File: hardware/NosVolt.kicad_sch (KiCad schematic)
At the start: 18 parts, among them J101 INPUTS, J102 OUTPUTS, SW101 SW_Reset, SW102 SSSS811101, U101 GMT028-05, U102 ESP32-S3-WROOM-1

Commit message: Test points
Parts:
- added C104: 100nF, Capacitor_SMD:C_0603_1608Metric, symbol Device:C
- added J103: BAT_NTC, Connector_JST:JST_GH_SM03B-GHS-TB_1x03-1MP_P1.25mm_Horizontal, symbol Connector_Generic_MountingPin:Conn_01x03_MountingPin
- added R105: 4.7K, Resistor_SMD:R_0603_1608Metric_Pad0.98x0.95mm_HandSolder, symbol Device:R
- added TP_101: BOOT, NosLib:TestPoint_Pad_1.0x1.0mm, symbol Connector:TestPoint
- added TP_102: +5V_USB, NosLib:TestPoint_Pad_1.0x1.0mm, symbol Connector:TestPoint
- added TP_103: SDA, NosLib:TestPoint_Pad_1.0x1.0mm, symbol Connector:TestPoint
- added TP_104: SCL, NosLib:TestPoint_Pad_1.0x1.0mm, symbol Connector:TestPoint
- added TP_105, TP_116: GND, NosLib:TestPoint_Pad_1.0x1.0mm, symbol Connector:TestPoint
- added TP_106: MTCK, NosLib:TestPoint_Pad_1.0x1.0mm, symbol Connector:TestPoint
- added TP_107: MTDO, NosLib:TestPoint_Pad_1.0x1.0mm, symbol Connector:TestPoint
- added TP_108: MTDI, NosLib:TestPoint_Pad_1.0x1.0mm, symbol Connector:TestPoint
- added TP_109: MTMS, NosLib:TestPoint_Pad_1.0x1.0mm, symbol Connector:TestPoint
- added TP_110: DALLAS, NosLib:TestPoint_Pad_1.0x1.0mm, symbol Connector:TestPoint
- added TP_112: TX, NosLib:TestPoint_Pad_1.0x1.0mm, symbol Connector:TestPoint
- added TP_113: RX, NosLib:TestPoint_Pad_1.0x1.0mm, symbol Connector:TestPoint
- added TP_115: +3V3_USB, NosLib:TestPoint_Pad_1.0x1.0mm, symbol Connector:TestPoint
- added TP_117: +3V3_UPS, NosLib:TestPoint_Pad_1.0x1.0mm, symbol Connector:TestPoint
- added TP_118: +12V_UPS, NosLib:TestPoint_Pad_1.0x1.0mm, symbol Connector:TestPoint
- added TP_123: +3V3, NosLib:TestPoint_Pad_1.0x1.0mm, symbol Connector:TestPoint
- added U102: DS18B20Z, Package_SO:SOIC-8_3.9x4.9mm_P1.27mm, symbol Sensor_Temperature:DS18B20Z
- renumbered U102 to U103
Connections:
- net SHUNT_OUT_LO is gone; now on net SHUNT_OUT_HI: J101.1 (Pin_1), NT101.2
- net +12V_UPS: now also TP_118.1
- net +3V3: now also C104.1, J103.3 (Pin_3), R105.2, TP_123.1, U102.3 (V_{DD})
- net +3V3_UPS: now also TP_117.1
- net +3V3_USB: now also TP_115.1
- net BOOT: now also TP_101.1
- net GND: now also C104.2, J103.1 (Pin_1), J103.MP (MountPin), TP_105.1, TP_116.1, U102.5 (GND)
- net SCL: now also TP_103.1
- net SDA: now also TP_104.1
- net SHUNT_OUT_HI: no longer J101.2 (Pin_2), J102.2 (Pin_2), J102.4 (Pin_4), J102.6 (Pin_6)
- net USB_LDO/USB_5V: now also TP_102.1
- net DALLAS: now reaches U103.31 (GPIO38/FSPIWP/SUBSPIWP)
- net DALLAS: now also J103.2 (Pin_2), R105.1, TP_110.1, U102.4 (DQ)
- net at U103.32 (MTCK/GPIO39/CLK_OUT3/SUBSPICS1): now also TP_106.1
- net at U103.33 (MTDO/GPIO40/CLK_OUT2): now also TP_107.1
- net at U103.34 (MTDI/GPIO41/CLK_OUT1): now also TP_108.1
- net at U103.35 (MTMS/GPIO42): now also TP_109.1
- net at U103.36 (U0RXD/GPIO44/CLK_OUT2): now also TP_113.1
- net at U103.37 (U0TXD/GPIO43/CLK_OUT1): now also TP_112.1
- net SHUNT_OUT_LO1 renamed SHUNT_USP_LO1
- net SHUNT_OUT_LO2 renamed SHUNT_LO_OUT2
- net SHUNT_OUT_LO3 renamed SHUNT_USP_LO3
- new net SHUNT_GND: J101.2 (Pin_2), J102.2 (Pin_2), J102.4 (Pin_4), J102.6 (Pin_6)
- no-connect marks 6 -> 11
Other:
- moved on the sheet: H101, H102, H103, H104, J101, J102, NT101, R101, R103, R104, U101, U103

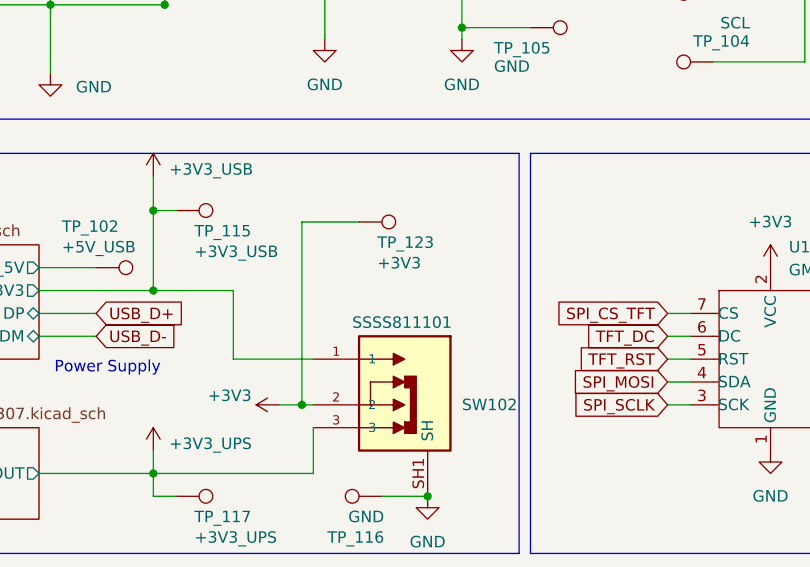
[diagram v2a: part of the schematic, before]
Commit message: hand soldering footprints and led
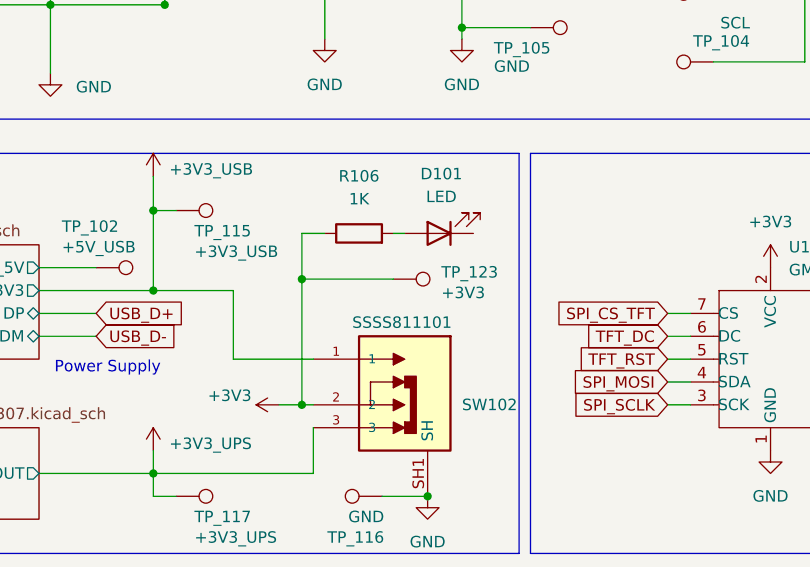
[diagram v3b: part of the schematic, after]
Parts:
- added D101: LED, LED_SMD:LED_0805_2012Metric_Pad1.15x1.40mm_HandSolder, symbol Device:LED
- added R106: 1K, Resistor_SMD:R_0603_1608Metric_Pad0.98x0.95mm_HandSolder, symbol Device:R
- C101, C103: footprint Capacitor_SMD:C_0805_2012Metric -> Capacitor_SMD:C_0805_2012Metric_Pad1.18x1.45mm_HandSolder
- C102, C104: footprint Capacitor_SMD:C_0603_1608Metric -> Capacitor_SMD:C_0603_1608Metric_Pad1.08x0.95mm_HandSolder
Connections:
- net +3V3: now also R106.1
- new net: D101.2 (A), R106.2
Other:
- moved on the sheet: TP_123
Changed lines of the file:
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@@
 	)
 	(junction
+		(at 85.09 76.2)
+		(diameter 0)
+		(color 0 0 0 0)
+	)
+	(junction
 		(at 119.38 30.48)
 		(diameter 0)
@@
 	(wire
 		(pts
+			(xy 95.25 71.12) (xy 96.52 71.12)
+		)
+		(stroke
+			(width 0)
+			(type default)
+		)
+	)
+	(wire
+		(pts
 			(xy 35.56 163.83) (xy 35.56 170.18)
 		)
@@
 	(wire
 		(pts
+			(xy 85.09 71.12) (xy 85.09 76.2)
+		)
+		(stroke
+			(width 0)
+			(type default)
+		)
+	)
+	(wire
+		(pts
 			(xy 140.97 52.07) (xy 140.97 30.48)
 		)
@@
 	(wire
 		(pts
-			(xy 91.44 69.85) (xy 85.09 69.85)
+			(xy 95.25 76.2) (xy 85.09 76.2)
 		)
 		(stroke
@@
 	(wire
 		(pts
-			(xy 85.09 69.85) (xy 85.09 90.17)
+			(xy 85.09 76.2) (xy 85.09 90.17)
 		)
 		(stroke
@@
 	(wire
 		(pts
+			(xy 87.63 71.12) (xy 85.09 71.12)
+		)
+		(stroke
+			(width 0)
+			(type default)
+		)
+	)
+	(wire
+		(pts
 			(xy 55.88 77.47) (xy 68.58 77.47)
 		)
@@
 			)
 		)
-		(property "Footprint" "Capacitor_SMD:C_0805_2012Metric"
+		(property "Footprint" "Capacitor_SMD:C_0805_2012Metric_Pad1.18x1.45mm_HandSolder"
 			(at 103.8352 44.45 0)
 			(effects
@@
 			)
 		)
-		(property "Footprint" "Capacitor_SMD:C_0805_2012Metric"
+		(property "Footprint" "Capacitor_SMD:C_0805_2012Metric_Pad1.18x1.45mm_HandSolder"
 			(at 58.1152 44.45 0)
 			(effects
@@
 	)
 	(symbol
+		(lib_id "Device:R")
+		(at 91.44 71.12 90)
+		(unit 1)
+		(exclude_from_sim no)
+		(in_bom yes)
+		(on_board yes)
+		(dnp no)
+		(fields_autoplaced yes)
+		(property "Reference" "R106"
+			(at 91.44 64.77 90)
+			(effects
+				(font
+					(size 1.27 1.27)
+				)
+			)
+		)
+		(property "Value" "1K"
+			(at 91.44 67.31 90)
+			(effects
+				(font
+					(size 1.27 1.27)
+				)
+			)
+		)
+		(property "Footprint" "Resistor_SMD:R_0603_1608Metric_Pad0.98x0.95mm_HandSolder"
+			(at 91.44 72.898 90)
+			(effects
+				(font
+					(size 1.27 1.27)
+				)
+				(hide yes)
+			)
+		)
+		(property "Datasheet" "~"
+			(at 91.44 71.12 0)
+			(effects
+				(font
+					(size 1.27 1.27)
+				)
+				(hide yes)
+			)
+		)
+		(property "Description" "Resistor"
+			(at 91.44 71.12 0)
+			(effects
+				(font
+					(size 1.27 1.27)
+				)
+				(hide yes)
+			)
+		)
+		(pin "2"
+		)
+		(pin "1"
+		)
+		(instances
+			(project "NosVolt"
+				(path "/2a3ef4c2-927a-45cd-a4f2-5ee83a7e9444"
+					(reference "R106")
+					(unit 1)
+				)
+			)
+		)
+	)
+	(symbol
 		(lib_id "NosLib:SSSS811101")
 		(at 96.52 87.63 0)
@@
 	(symbol
 		(lib_id "Connector:TestPoint")
-		(at 91.44 69.85 270)
+		(at 95.25 76.2 270)
 		(unit 1)
 		(exclude_from_sim no)
@@
 		(dnp no)
 		(property "Reference" "TP_123"
-			(at 93.472 72.136 90)
+			(at 100.584 75.438 90)
 			(effects
 				(font
@@
 		)
 		(property "Value" "+3V3"
-			(at 93.472 74.422 90)
+			(at 100.584 77.724 90)
 			(effects
 				(font
@@
 		)
 		(property "Footprint" "NosLib:TestPoint_Pad_1.0x1.0mm"
-			(at 91.44 74.93 0)
+			(at 95.25 81.28 0)
 			(effects
 				(font
@@
 		)
 		(property "Datasheet" "~"
-			(at 91.44 74.93 0)
+			(at 95.25 81.28 0)
 			(effects
 				(font
@@
 		)
 		(property "Description" "test point"
-			(at 91.44 69.85 0)
+			(at 95.25 76.2 0)
 			(effects
 				(font
@@
 	)
 	(symbol
+		(lib_id "Device:LED")
+		(at 100.33 71.12 180)
+		(unit 1)
+		(exclude_from_sim no)
+		(in_bom yes)
+		(on_board yes)
+		(dnp no)
+		(property "Reference" "D101"
+			(at 100.584 64.516 0)
+			(effects
+				(font
+					(size 1.27 1.27)
+				)
+			)
+		)
+		(property "Value" "LED"
+			(at 100.584 67.056 0)
+			(effects
+				(font
+					(size 1.27 1.27)
+				)
+			)
+		)
+		(property "Footprint" "LED_SMD:LED_0805_2012Metric_Pad1.15x1.40mm_HandSolder"
+			(at 100.33 71.12 0)
+			(effects
+				(font
+					(size 1.27 1.27)
+				)
+				(hide yes)
+			)
+		)
+		(property "Datasheet" "~"
+			(at 100.33 71.12 0)
+			(effects
+				(font
+					(size 1.27 1.27)
+				)
+				(hide yes)
+			)
+		)
+		(property "Description" "Light emitting diode"
+			(at 100.33 71.12 0)
+			(effects
+				(font
+					(size 1.27 1.27)
+				)
+				(hide yes)
+			)
+		)
+		(property "Sim.Pins" "1=K 2=A"
+			(at 100.33 71.12 0)
+			(effects
+				(font
+					(size 1.27 1.27)
+				)
+				(hide yes)
+			)
+		)
+		(pin "2"
+		)
+		(pin "1"
+		)
+		(instances
+			(project ""
+				(path "/2a3ef4c2-927a-45cd-a4f2-5ee83a7e9444"
+					(reference "D101")
+					(unit 1)
+				)
+			)
+		)
+	)
+	(symbol
 		(lib_id "power:+3.3V")
 		(at 68.58 64.77 0)
@@
 			)
 		)
-		(property "Footprint" "Capacitor_SMD:C_0603_1608Metric"
+		(property "Footprint" "Capacitor_SMD:C_0603_1608Metric_Pad1.08x0.95mm_HandSolder"
 			(at 199.39 152.7048 0)
 			(effects
@@
 			)
 		)
-		(property "Footprint" "Capacitor_SMD:C_0603_1608Metric"
+		(property "Footprint" "Capacitor_SMD:C_0603_1608Metric_Pad1.08x0.95mm_HandSolder"
 			(at 88.5952 44.45 0)
 			(effects

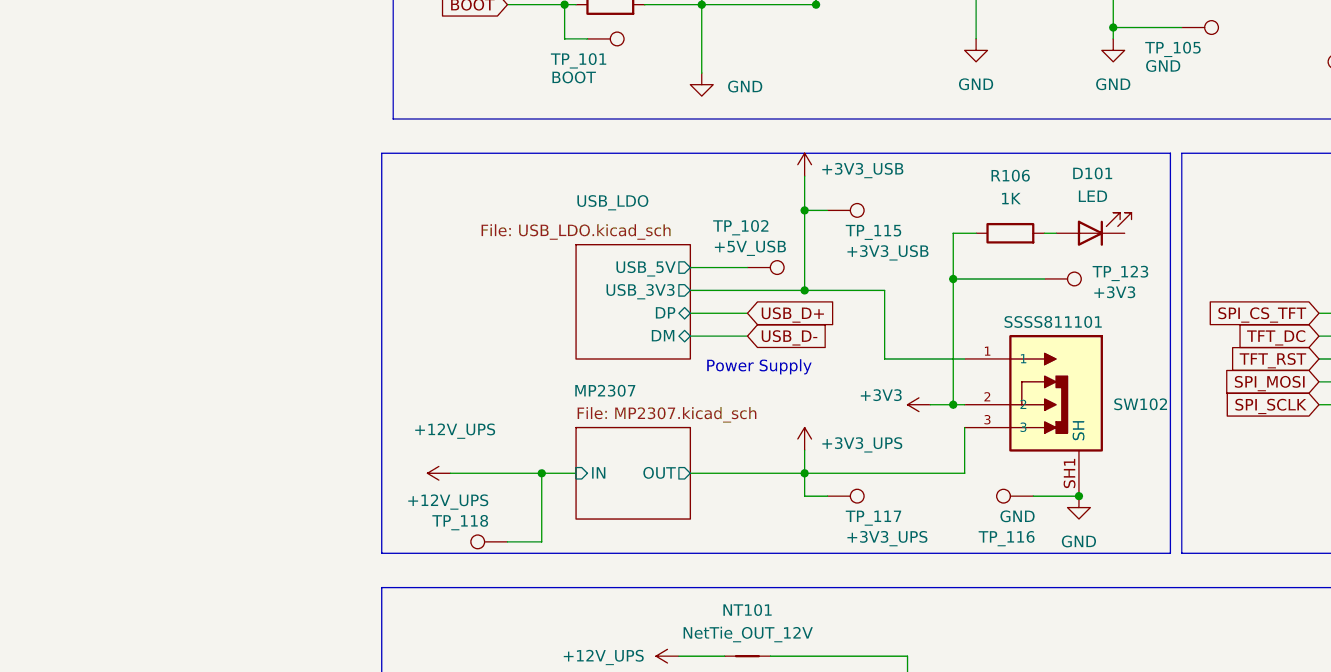
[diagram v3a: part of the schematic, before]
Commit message: hand soldering footprints and led
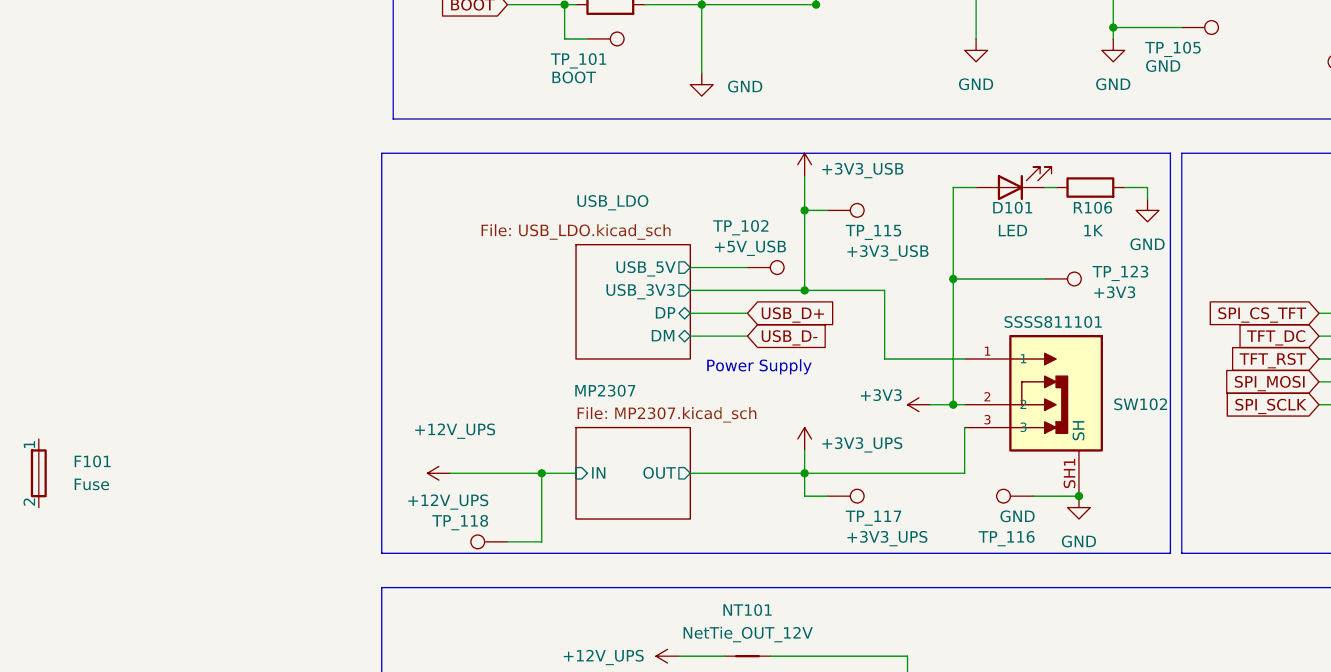
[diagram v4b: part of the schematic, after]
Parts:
- added F101: Fuse, NosLib:FUSE_3544-2, symbol Device:Fuse
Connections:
- net +3V3: now also D101.2 (A); no longer R106.1
- net GND: now also R106.2
- net at D101.1 (K): now also R106.1
- new net: F101.1_1 (1), F101.1_2 (1)
- new net: F101.2_1 (2), F101.2_2 (2)
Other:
- moved on the sheet: D101, R106
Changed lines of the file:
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@@
 	(wire
 		(pts
-			(xy 95.25 71.12) (xy 96.52 71.12)
+			(xy 95.25 66.04) (xy 96.52 66.04)
+		)
+		(stroke
+			(width 0)
+			(type default)
+		)
+	)
+	(wire
+		(pts
+			(xy 106.68 66.04) (xy 104.14 66.04)
 		)
 		(stroke
@@
 	(wire
 		(pts
-			(xy 85.09 71.12) (xy 85.09 76.2)
+			(xy 85.09 66.04) (xy 85.09 76.2)
 		)
 		(stroke
@@
 	(wire
 		(pts
+			(xy 106.68 66.04) (xy 106.68 67.31)
+		)
+		(stroke
+			(width 0)
+			(type default)
+		)
+	)
+	(wire
+		(pts
 			(xy 80.01 176.53) (xy 80.01 152.4)
 		)
@@
 	(wire
 		(pts
-			(xy 87.63 71.12) (xy 85.09 71.12)
+			(xy 87.63 66.04) (xy 85.09 66.04)
 		)
 		(stroke
@@
 	(symbol
 		(lib_id "Device:R")
-		(at 91.44 71.12 90)
+		(at 100.33 66.04 90)
 		(unit 1)
 		(exclude_from_sim no)
@@
 		(on_board yes)
 		(dnp no)
-		(fields_autoplaced yes)
 		(property "Reference" "R106"
-			(at 91.44 64.77 90)
+			(at 100.584 68.326 90)
 			(effects
 				(font
@@
 		)
 		(property "Value" "1K"
-			(at 91.44 67.31 90)
+			(at 100.584 70.866 90)
 			(effects
 				(font
@@
 		)
 		(property "Footprint" "Resistor_SMD:R_0603_1608Metric_Pad0.98x0.95mm_HandSolder"
-			(at 91.44 72.898 90)
+			(at 100.33 67.818 90)
 			(effects
 				(font
@@
 		)
 		(property "Datasheet" "~"
-			(at 91.44 71.12 0)
+			(at 100.33 66.04 0)
 			(effects
 				(font
@@
 		)
 		(property "Description" "Resistor"
-			(at 91.44 71.12 0)
+			(at 100.33 66.04 0)
 			(effects
 				(font
@@
 	(symbol
 		(lib_id "Device:LED")
-		(at 100.33 71.12 180)
+		(at 91.44 66.04 180)
 		(unit 1)
 		(exclude_from_sim no)
@@
 		(dnp no)
 		(property "Reference" "D101"
-			(at 100.584 64.516 0)
+			(at 91.694 68.326 0)
 			(effects
 				(font
@@
 		)
 		(property "Value" "LED"
-			(at 100.584 67.056 0)
+			(at 91.694 70.866 0)
 			(effects
 				(font
@@
 		)
 		(property "Footprint" "LED_SMD:LED_0805_2012Metric_Pad1.15x1.40mm_HandSolder"
-			(at 100.33 71.12 0)
+			(at 91.44 66.04 0)
 			(effects
 				(font
@@
 		)
 		(property "Datasheet" "~"
-			(at 100.33 71.12 0)
+			(at 91.44 66.04 0)
 			(effects
 				(font
@@
 		)
 		(property "Description" "Light emitting diode"
-			(at 100.33 71.12 0)
+			(at 91.44 66.04 0)
 			(effects
 				(font
@@
 		)
 		(property "Sim.Pins" "1=K 2=A"
-			(at 100.33 71.12 0)
+			(at 91.44 66.04 0)
 			(effects
 				(font
@@
 		)
 		(instances
-			(project ""
+			(project "NosVolt"
 				(path "/2a3ef4c2-927a-45cd-a4f2-5ee83a7e9444"
 					(reference "D101")
@@
 	)
 	(symbol
+		(lib_id "Device:Fuse")
+		(at -16.51 97.79 0)
+		(unit 1)
+		(exclude_from_sim no)
+		(in_bom yes)
+		(on_board yes)
+		(dnp no)
+		(fields_autoplaced yes)
+		(property "Reference" "F101"
+			(at -12.7 96.5199 0)
+			(effects
+				(font
+					(size 1.27 1.27)
+				)
+				(justify left)
+			)
+		)
+		(property "Value" "Fuse"
+			(at -12.7 99.0599 0)
+			(effects
+				(font
+					(size 1.27 1.27)
+				)
+				(justify left)
+			)
+		)
+		(property "Footprint" "NosLib:FUSE_3544-2"
+			(at -18.288 97.79 90)
+			(effects
+				(font
+					(size 1.27 1.27)
+				)
+				(hide yes)
+			)
+		)
+		(property "Datasheet" "~"
+			(at -16.51 97.79 0)
+			(effects
+				(font
+					(size 1.27 1.27)
+				)
+				(hide yes)
+			)
+		)
+		(property "Description" "Fuse"
+			(at -16.51 97.79 0)
+			(effects
+				(font
+					(size 1.27 1.27)
+				)
+				(hide yes)
+			)
+		)
+		(pin "2_1"
+		)
+		(pin "1_2"
+		)
+		(pin "2_2"
+		)
+		(pin "1_1"
+		)
+		(instances
+			(project ""
+				(path "/2a3ef4c2-927a-45cd-a4f2-5ee83a7e9444"
+					(reference "F101")
+					(unit 1)
+				)
+			)
+		)
+	)
+	(symbol
 		(lib_id "Connector_Generic_MountingPin:Conn_01x03_MountingPin")
 		(at 173.99 143.51 0)
@@
 					(unit 1)
 				)
+			)
+		)
+	)
+	(symbol
+		(lib_id "power:GND")
+		(at 106.68 67.31 0)
+		(unit 1)
+		(exclude_from_sim no)
+		(in_bom yes)
+		(on_board yes)
+		(dnp no)
+		(fields_autoplaced yes)
+		(property "Reference" "#PWR0123"
+			(at 106.68 73.66 0)
+			(effects
+				(font
+					(size 1.27 1.27)
+				)
+				(hide yes)
+			)
+		)
+		(property "Value" "GND"
+			(at 106.68 72.39 0)
+			(effects
+				(font
+					(size 1.27 1.27)
+				)
+			)
+		)
+		(property "Footprint" ""
+			(at 106.68 67.31 0)
+			(effects
+				(font
+					(size 1.27 1.27)
+				)
+				(hide yes)
+			)
+		)
+		(property "Datasheet" ""
+			(at 106.68 67.31 0)
+			(effects
+				(font
+					(size 1.27 1.27)
+				)
+				(hide yes)
+			)
+		)
+		(property "Description" "Power symbol creates a global label with name \"GND\" , ground"
+			(at 106.68 67.31 0)
+			(effects
+				(font
+					(size 1.27 1.27)
+				)
+				(hide yes)
+			)
+		)
+		(pin "1"
+		)
+		(instances
+			(project "NosVolt"
+				(path "/2a3ef4c2-927a-45cd-a4f2-5ee83a7e9444"
+					(reference "#PWR0123")
+					(unit 1)
+				)

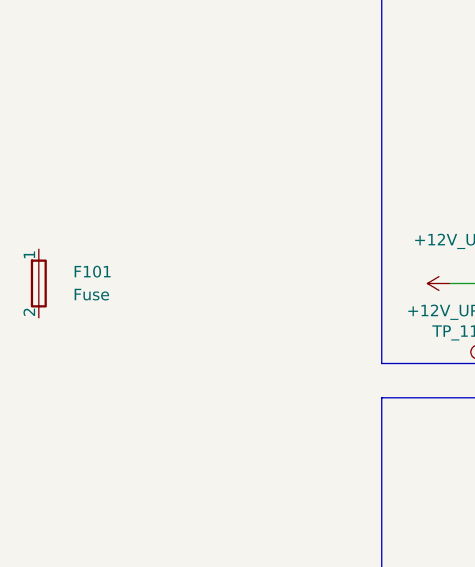
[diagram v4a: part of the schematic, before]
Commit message: remove fuse
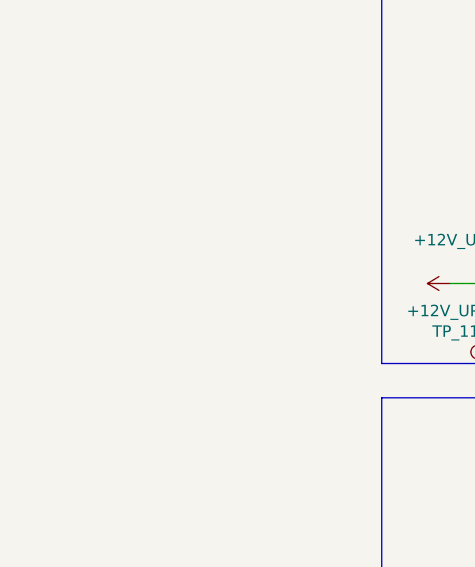
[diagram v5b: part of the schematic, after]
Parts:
- removed F101: Fuse, NosLib:FUSE_3544-2, symbol Device:Fuse
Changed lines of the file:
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@@
-	)
-	(symbol
-		(lib_id "Device:Fuse")
-		(at -16.51 97.79 0)
-		(unit 1)
-		(exclude_from_sim no)
-		(in_bom yes)
-		(on_board yes)
-		(dnp no)
-		(fields_autoplaced yes)
-		(property "Reference" "F101"
-			(at -12.7 96.5199 0)
-			(effects
-				(font
-					(size 1.27 1.27)
-				)
-				(justify left)
-			)
-		)
-		(property "Value" "Fuse"
-			(at -12.7 99.0599 0)
-			(effects
-				(font
-					(size 1.27 1.27)
-				)
-				(justify left)
-			)
-		)
-		(property "Footprint" "NosLib:FUSE_3544-2"
-			(at -18.288 97.79 90)
-			(effects
-				(font
-					(size 1.27 1.27)
-				)
-				(hide yes)
-			)
-		)
-		(property "Datasheet" "~"
-			(at -16.51 97.79 0)
-			(effects
-				(font
-					(size 1.27 1.27)
-				)
-				(hide yes)
-			)
-		)
-		(property "Description" "Fuse"
-			(at -16.51 97.79 0)
-			(effects
-				(font
-					(size 1.27 1.27)
-				)
-				(hide yes)
-			)
-		)
-		(pin "2_1"
-		)
-		(pin "1_2"
-		)
-		(pin "2_2"
-		)
-		(pin "1_1"
-		)
-		(instances
-			(project ""
-				(path "/2a3ef4c2-927a-45cd-a4f2-5ee83a7e9444"
-					(reference "F101")
-					(unit 1)
-				)
-			)
-		)
 	)
 	(symbol
